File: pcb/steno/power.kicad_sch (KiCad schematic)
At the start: 14 parts, among them J2 USB_C_Receptacle_USB2.0, SW1 SW_SPDT, U4 BQ24075, U5 XC6206B331MR, U6 SRV05-4

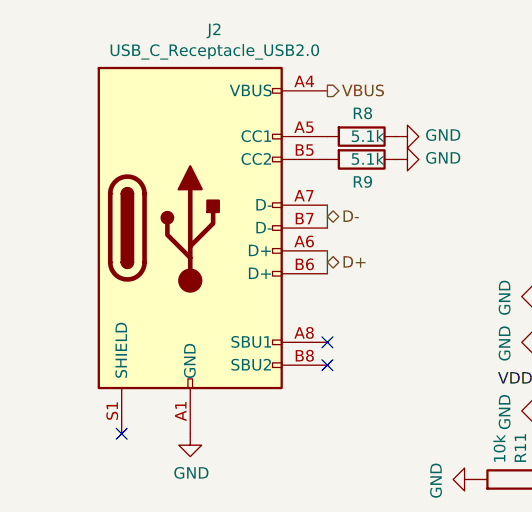
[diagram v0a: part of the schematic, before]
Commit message: [pcb] auklet 3: use new libraries
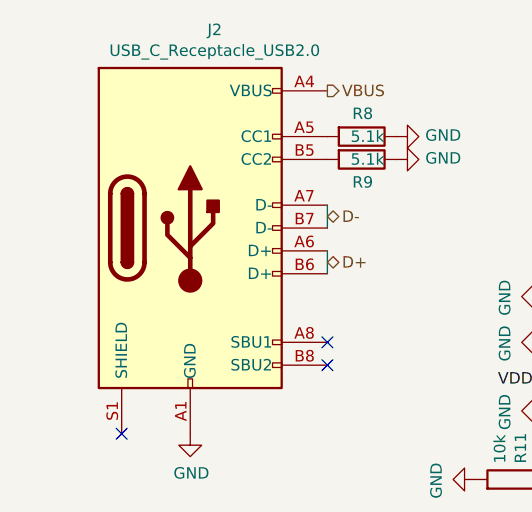
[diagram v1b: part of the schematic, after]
